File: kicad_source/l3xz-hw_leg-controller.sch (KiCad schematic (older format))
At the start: 23 parts, among them CN1 ARDUINO_NANO_33, CN2 SM04B-SRSS-TB, CN3 SM04B-SRSS-TB, CN6 CONN_02X03, P1 CONN_01X02, U3 24LC64

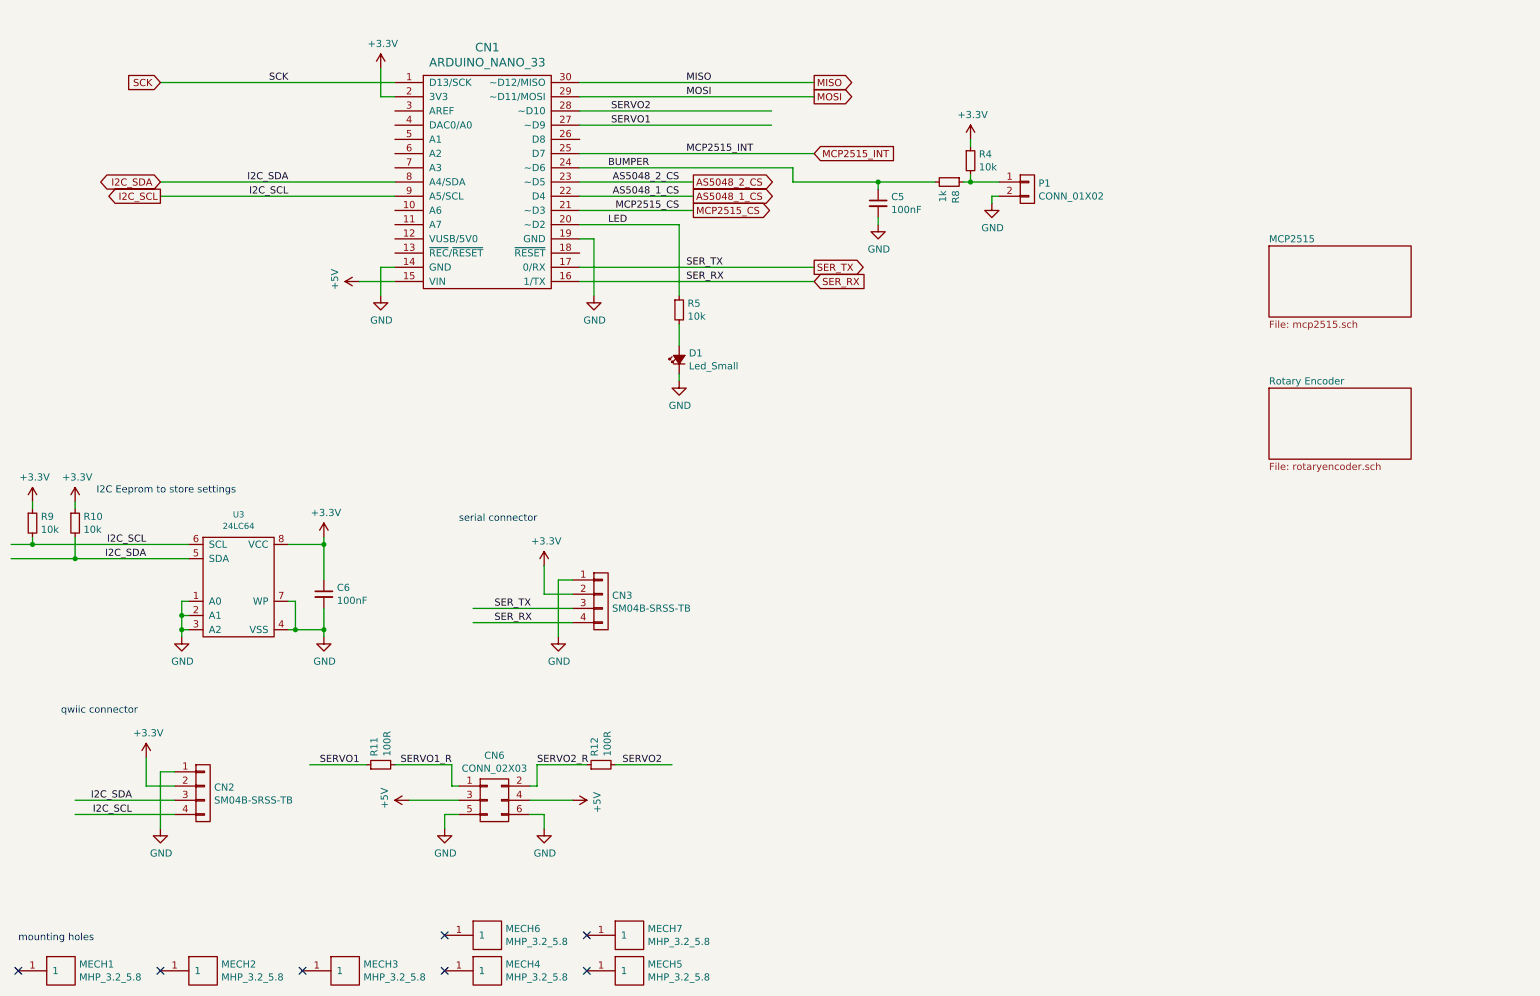
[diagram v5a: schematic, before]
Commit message: updated connectors, added power input
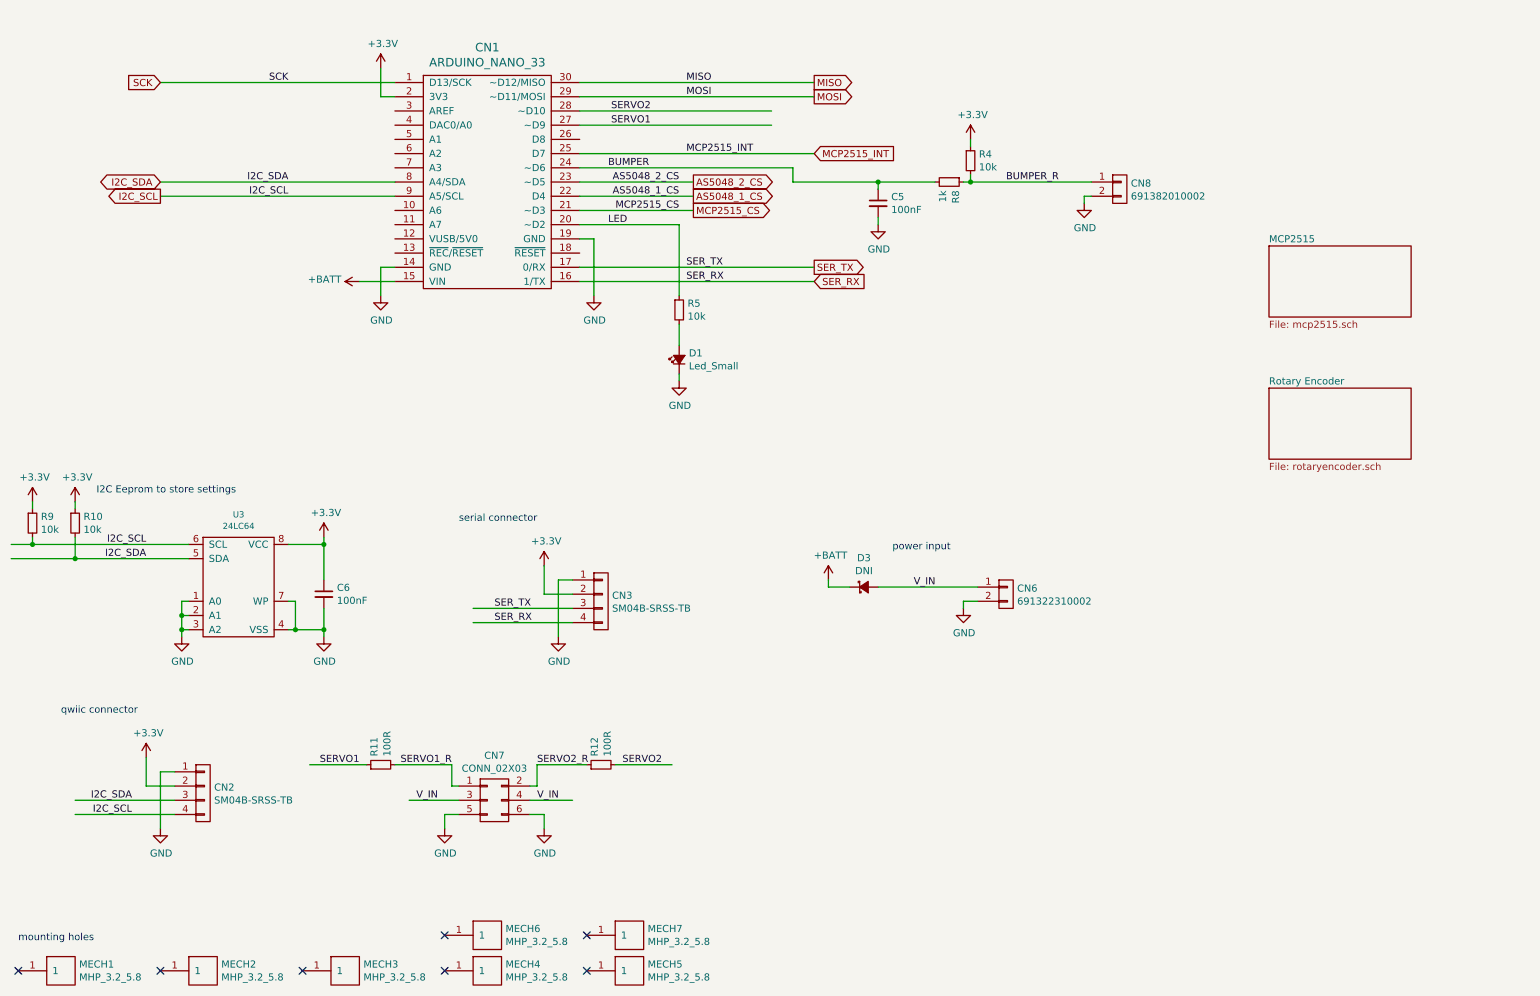
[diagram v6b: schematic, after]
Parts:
- added CN6: 691322310002, CON_wuerth:WR-TBL_691322310002, symbol mechanical-connectors:CONN_01X02
- added D3: DNI, diodes:SOD-123, symbol devices:D_Schottky_Small
- CN8: renamed from P1; value CONN_01X02 -> 691382010002; footprint CON_wuerth:WR-TBL_691382000002 -> CON_wuerth:WR-TBL_691382010002
- renumbered CN6 to CN7
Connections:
- net labels added: +BATT, BUMPER_R, V_IN
- net labels removed: +5V
- wire segments 85 -> 90
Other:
- note added: "power input"
- moved on the sheet: CN8
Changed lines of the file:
@@
 	5350 3400 5350 3450
 $Comp
-L mechanical-connectors:CONN_01X02 P1
+L mechanical-connectors:CONN_01X02 CN8
 U 1 1 624C3078
-P 7800 2100
-F 0 "P1" H 7878 2141 50  0000 L CNN
-F 1 "CONN_01X02" H 7878 2050 50  0000 L CNN
-F 2 "CON_wuerth:WR-TBL_691382000002" H 7878 2004 50  0001 L CNN
-F 3 "" H 7800 2100 50  0000 C CNN
-	1    7800 2100
+P 8450 2100
+F 0 "CN8" H 8528 2141 50  0000 L CNN
+F 1 "691382010002" H 8528 2050 50  0000 L CNN
+F 2 "CON_wuerth:WR-TBL_691382010002" H 8528 2004 50  0001 L CNN
+F 3 "" H 8450 2100 50  0000 C CNN
+	1    8450 2100
 	1    0    0    -1
 $EndComp
@@
 L power-supply:GND #PWR04
 U 1 1 624C581E
-P 7550 2200
-F 0 "#PWR04" H 7550 1950 50  0001 C CNN
-F 1 "GND" H 7555 2027 50  0000 C CNN
-F 2 "" H 7550 2200 50  0000 C CNN
-F 3 "" H 7550 2200 50  0000 C CNN
-	1    7550 2200
-	1    0    0    -1
-$EndComp
-Wire Wire Line
-	7600 2050 7400 2050
+P 8200 2200
+F 0 "#PWR04" H 8200 1950 50  0001 C CNN
+F 1 "GND" H 8205 2027 50  0000 C CNN
+F 2 "" H 8200 2200 50  0000 C CNN
+F 3 "" H 8200 2200 50  0000 C CNN
+	1    8200 2200
+	1    0    0    -1
+$EndComp
 Wire Wire Line
 	6150 2050 6150 1950
@@
 	7400 2000 7400 2050
 Wire Wire Line
-	7550 2150 7550 2200
-Wire Wire Line
-	7600 2150 7550 2150
+	8200 2150 8200 2200
+Wire Wire Line
+	8250 2150 8200 2150
 Text Label 4850 2350 0    50   ~ 0
 LED
@@
 qwiic connector
 $Comp
-L mechanical-connectors:CONN_02X03 CN6
+L mechanical-connectors:CONN_02X03 CN7
 U 1 1 624F7225
 P 4050 6400
-F 0 "CN6" H 4050 6715 50  0000 C CNN
+F 0 "CN7" H 4050 6715 50  0000 C CNN
 F 1 "CONN_02X03" H 4050 6624 50  0000 C CNN
 F 2 "pin_headers:Pin_Header_Angled_2x03" H 4050 5200 50  0001 C CNN
@@
 	1    0    0    -1
 $EndComp
-$Comp
-L power-supply:+5V #PWR?
-U 1 1 624FA729
-P 3100 2750
-AR Path="/624F7A5F/624FA729" Ref="#PWR?"  Part="1"
-AR Path="/5ED92F9C/624FA729" Ref="#PWR?"  Part="1"
-AR Path="/624FA729" Ref="#PWR015"  Part="1"
-F 0 "#PWR015" H 3100 2600 50  0001 C CNN
-F 1 "+5V" H 3115 2923 50  0000 C CNN
-F 2 "" H 3100 2750 50  0000 C CNN
-F 3 "" H 3100 2750 50  0000 C CNN
-	1    3100 2750
-	0    -1   -1   0
-$EndComp
 Wire Wire Line
 	3350 2750 3100 2750
-$Comp
-L power-supply:+5V #PWR?
-U 1 1 624FB677
-P 3450 6400
-AR Path="/624F7A5F/624FB677" Ref="#PWR?"  Part="1"
-AR Path="/5ED92F9C/624FB677" Ref="#PWR?"  Part="1"
-AR Path="/624FB677" Ref="#PWR020"  Part="1"
-F 0 "#PWR020" H 3450 6250 50  0001 C CNN
-F 1 "+5V" H 3465 6573 50  0000 C CNN
-F 2 "" H 3450 6400 50  0000 C CNN
-F 3 "" H 3450 6400 50  0000 C CNN
-	1    3450 6400
-	0    -1   -1   0
-$EndComp
-$Comp
-L power-supply:+5V #PWR?
-U 1 1 624FC70C
-P 4600 6400
-AR Path="/624F7A5F/624FC70C" Ref="#PWR?"  Part="1"
-AR Path="/5ED92F9C/624FC70C" Ref="#PWR?"  Part="1"
-AR Path="/624FC70C" Ref="#PWR021"  Part="1"
-F 0 "#PWR021" H 4600 6250 50  0001 C CNN
-F 1 "+5V" H 4615 6573 50  0000 C CNN
-F 2 "" H 4600 6400 50  0000 C CNN
-F 3 "" H 4600 6400 50  0000 C CNN
-	1    4600 6400
-	0    1    1    0
-$EndComp
 $Comp
 L power-supply:GND #PWR032
@@
 Wire Wire Line
 	7350 2050 7400 2050
-Connection ~ 7400 2050
 Wire Wire Line
 	6750 2100 6750 2050
@@
 Text Label 3750 6150 2    50   ~ 0
 SERVO1_R
+$Comp
+L mechanical-connectors:CONN_01X02 CN6
+U 1 1 6252CED3
+P 7650 4950
+F 0 "CN6" H 7728 4991 50  0000 L CNN
+F 1 "691322310002" H 7728 4900 50  0000 L CNN
+F 2 "CON_wuerth:WR-TBL_691322310002" H 7728 4854 50  0001 L CNN
+F 3 "" H 7650 4950 50  0000 C CNN
+	1    7650 4950
+	1    0    0    -1
+$EndComp
+$Comp
+L power-supply:GND #PWR021
+U 1 1 6252DC09
+P 7350 5050
+F 0 "#PWR021" H 7350 4800 50  0001 C CNN
+F 1 "GND" H 7355 4877 50  0000 C CNN
+F 2 "" H 7350 5050 50  0000 C CNN
+F 3 "" H 7350 5050 50  0000 C CNN
+	1    7350 5050
+	1    0    0    -1
+$EndComp
+Text Notes 6850 4650 0    50   ~ 0
+power input
+$Comp
+L devices:D_Schottky_Small D?
+U 1 1 62533088
+P 6650 4900
+AR Path="/624F7A5F/62533088" Ref="D?"  Part="1"
+AR Path="/5ED92F9C/62533088" Ref="D?"  Part="1"
+AR Path="/62533088" Ref="D3"  Part="1"
+F 0 "D3" H 6650 5105 50  0000 C CNN
+F 1 "DNI" H 6650 5014 50  0000 C CNN
+F 2 "diodes:SOD-123" V 6650 4900 50  0001 C CNN
+F 3 "" V 6650 4900 50  0000 C CNN
+	1    6650 4900
+	1    0    0    -1
+$EndComp
+Wire Wire Line
+	7450 4900 6750 4900
+Wire Wire Line
+	6550 4900 6400 4900
+Wire Wire Line
+	6400 4900 6400 4850
+Text Label 7000 4900 0    50   ~ 0
+V_IN
+$Comp
+L power-supply:+BATT #PWR?
+U 1 1 62533092
+P 6400 4850
+AR Path="/5ED92F9C/62533092" Ref="#PWR?"  Part="1"
+AR Path="/62533092" Ref="#PWR020"  Part="1"
+F 0 "#PWR020" H 6400 4700 50  0001 C CNN
+F 1 "+BATT" H 6415 5023 50  0000 C CNN
+F 2 "" H 6400 4850 50  0000 C CNN
+F 3 "" H 6400 4850 50  0000 C CNN
+	1    6400 4850
+	1    0    0    -1
+$EndComp
+Wire Wire Line
+	7350 5000 7350 5050
+Wire Wire Line
+	7350 5000 7450 5000
+Wire Wire Line
+	7400 2050 8250 2050
+Connection ~ 7400 2050
+Text Label 7650 2050 0    50   ~ 0
+BUMPER_R
+$Comp
+L power-supply:+BATT #PWR?
+U 1 1 6254A49E
+P 3100 2750
+AR Path="/5ED92F9C/6254A49E" Ref="#PWR?"  Part="1"
+AR Path="/6254A49E" Ref="#PWR015"  Part="1"
+F 0 "#PWR015" H 3100 2600 50  0001 C CNN
+F 1 "+BATT" V 3115 2877 50  0000 L CNN
+F 2 "" H 3100 2750 50  0000 C CNN
+F 3 "" H 3100 2750 50  0000 C CNN
+	1    3100 2750
+	0    -1   -1   0
+$EndComp
+Text Label 4350 6400 0    50   ~ 0
+V_IN
+Text Label 3500 6400 0    50   ~ 0
+V_IN
 $EndSCHEMATC

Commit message: added additional leds, input measurement buffer capacitors
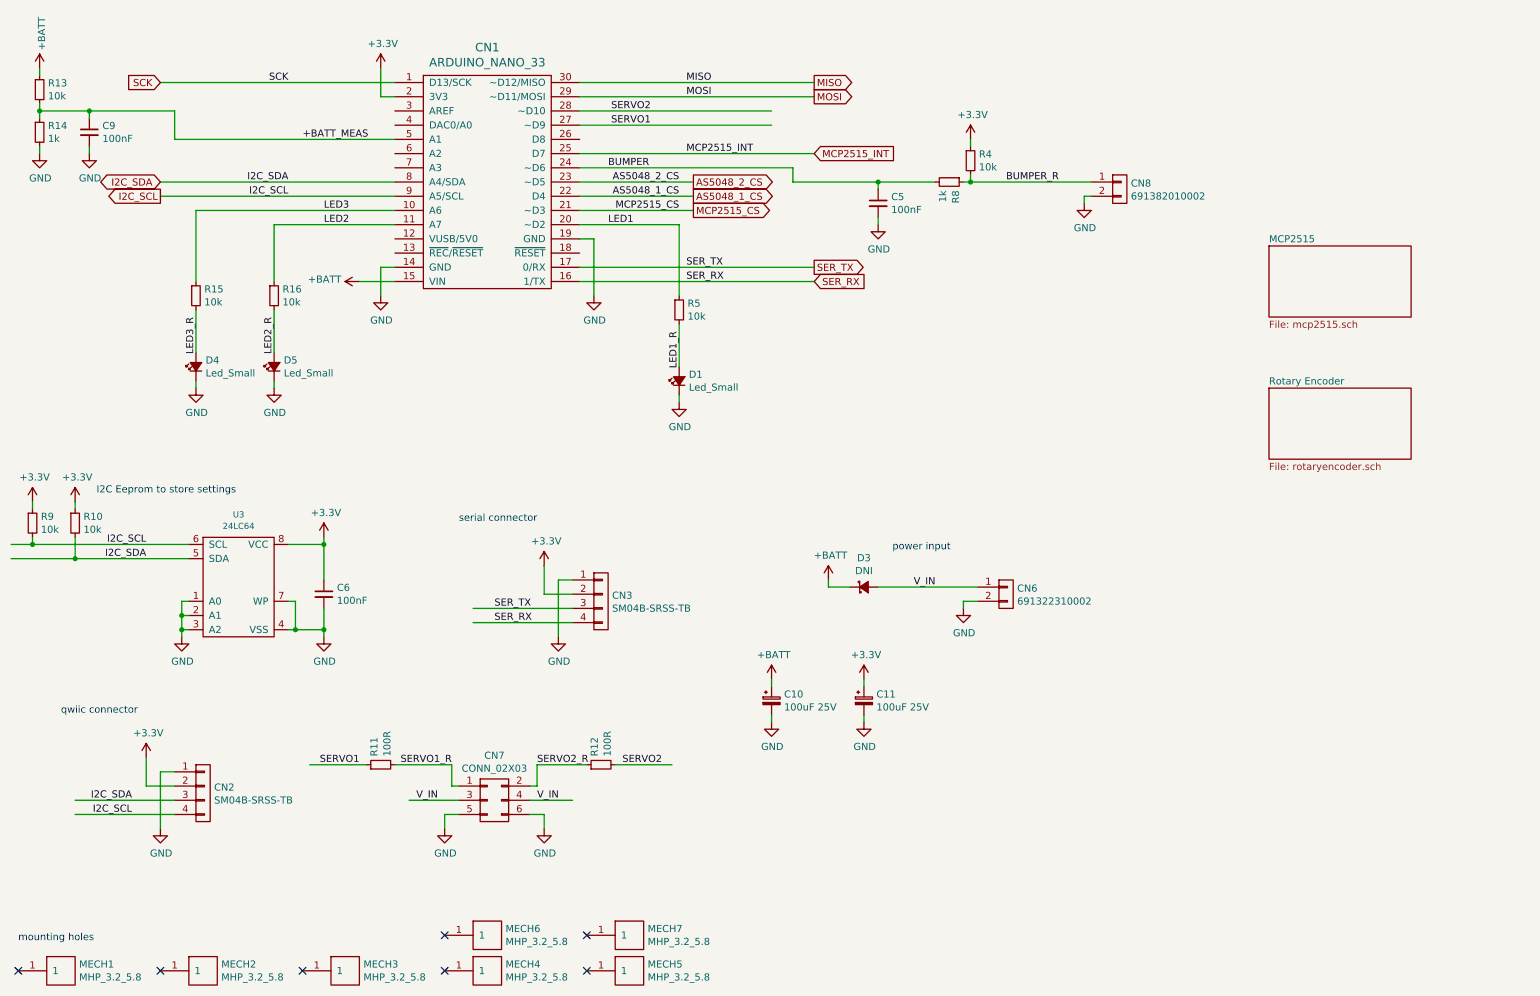
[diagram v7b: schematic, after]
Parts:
- added C10, C11: 100uF 25V, capacitors:c_elec_8x10, symbol devices:CP_Small
- added C9: 100nF, capacitors:C_0603, symbol devices:C_0603
- added D4, D5: Led_Small, LEDs:LED_0603, symbol devices:Led_Small
- added R13, R15, R16: 10k, resistors:R_0603, symbol devices:R_0603
- added R14: 1k, resistors:R_0603, symbol devices:R_0603
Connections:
- net labels added: +BATT_MEAS, LED1, LED1_R, LED2, LED2_R, LED3, LED3_R
- net labels removed: LED
- wire segments 90 -> 112
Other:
- moved on the sheet: D1

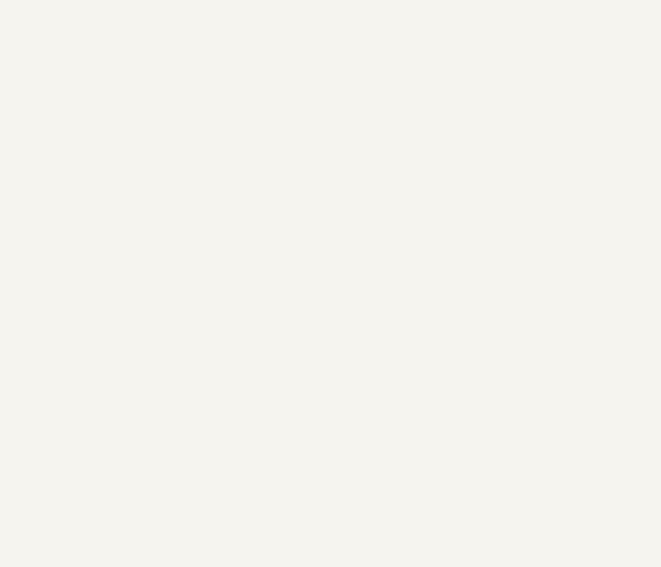
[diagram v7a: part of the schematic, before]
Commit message: added labels, beautified layout
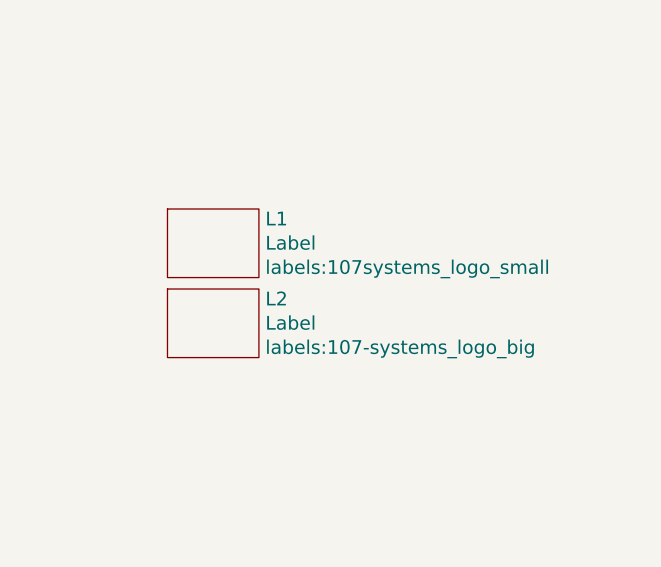
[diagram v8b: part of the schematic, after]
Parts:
- added L1: Label, labels:107systems_logo_small, symbol devices:Label
- added L2: Label, labels:107-systems_logo_big, symbol devices:Label
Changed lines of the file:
@@
 Sheet 1 3
 Title "l3xz-hw_leg-controller"
-Date "2022-04-08"
+Date "2022-04-10"
 Rev "0.1"
 Comp "107-systems"
@@
 	1    0    0    -1
 $EndComp
+$Comp
+L devices:Label L1
+U 1 1 625BB6FE
+P 9450 5250
+F 0 "L1" H 9678 5356 60  0000 L CNN
+F 1 "Label" H 9678 5250 60  0000 L CNN
+F 2 "labels:107systems_logo_small" H 9678 5144 60  0000 L CNN
+F 3 "" H 9450 5250 60  0000 C CNN
+	1    9450 5250
+	1    0    0    -1
+$EndComp
+$Comp
+L devices:Label L2
+U 1 1 625CACB9
+P 9450 5600
+F 0 "L2" H 9678 5706 60  0000 L CNN
+F 1 "Label" H 9678 5600 60  0000 L CNN
+F 2 "labels:107-systems_logo_big" H 9678 5494 60  0000 L CNN
+F 3 "" H 9450 5600 60  0000 C CNN
+	1    9450 5600
+	1    0    0    -1
+$EndComp
